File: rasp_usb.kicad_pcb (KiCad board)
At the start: 2 copper layers, 24 x 22 mm, 20 parts, among them J1 USB_B_Micro, J2 Conn_02x05_Odd_Even, U1 AMS1117-5.0, U2 FT230XQ

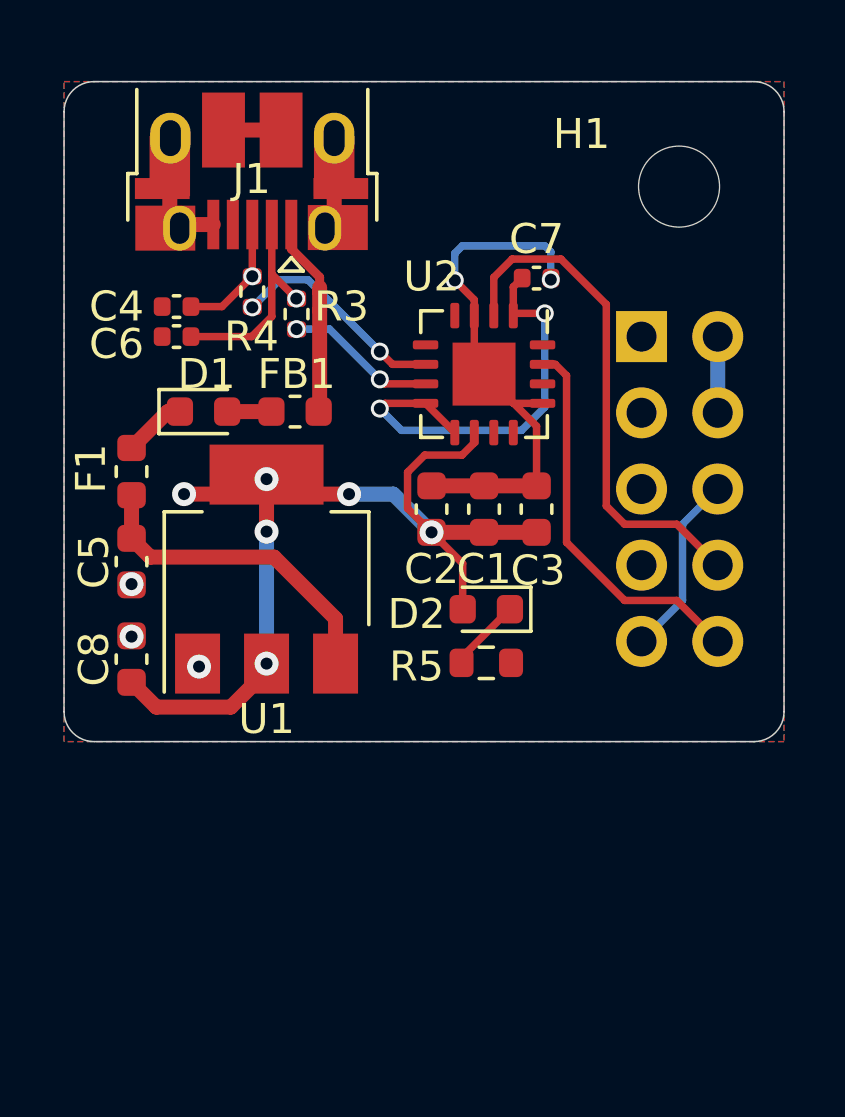
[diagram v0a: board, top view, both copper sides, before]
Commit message: ftdi ic is out of stock
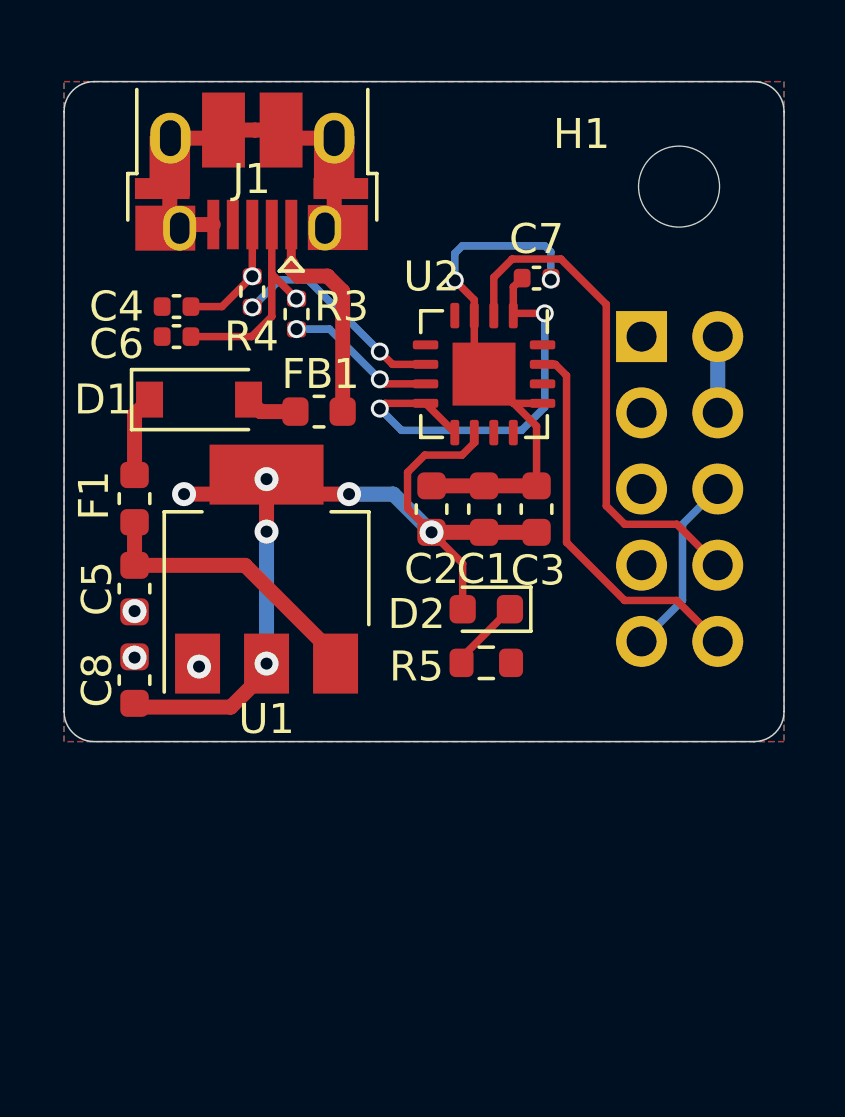
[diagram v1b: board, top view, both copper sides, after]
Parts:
- D1: footprint Diode_SMD:D_0603_1608Metric -> Diode_SMD:D_SOD-123
- moved C5 0.91 mm to (103.3, 76.9)
- moved F1 0.91 mm to (103.3, 73.9)
- moved FB1 0.80 mm to (109.5, 71.0)
- moved C8 0.71 mm to (103.3, 80.0)
- moved D1 0.43 mm to (105.5, 70.6)
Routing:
- net GND: track 33.4 -> 37.2 mm
- net Net-(C5-Pad1): track 10.9 -> 9.73 mm
- net VBUS: track 6.68 -> 7.52 mm
- net Net-(D1-Pad1): track 2.11 -> 2.72 mm

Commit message: ready to order
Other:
- board text added: "."

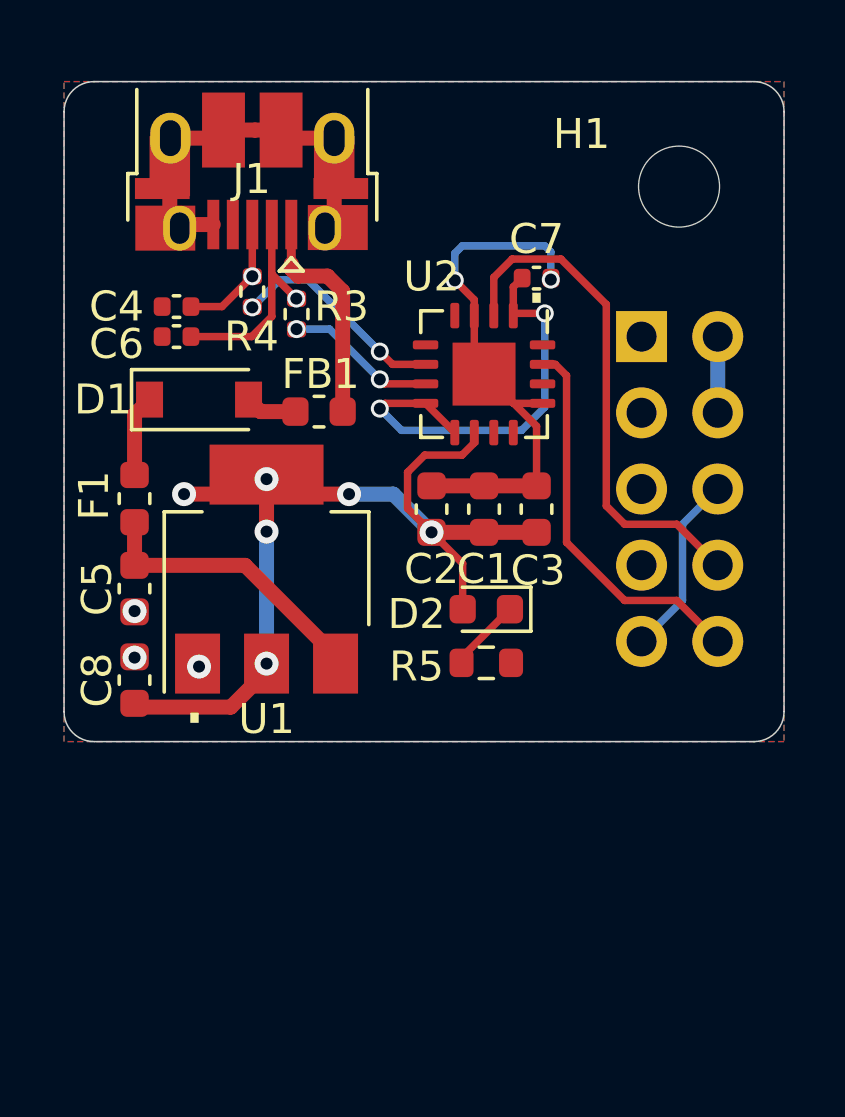
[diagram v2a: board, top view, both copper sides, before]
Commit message: Replaced usb IC with cp2104. Ready to order
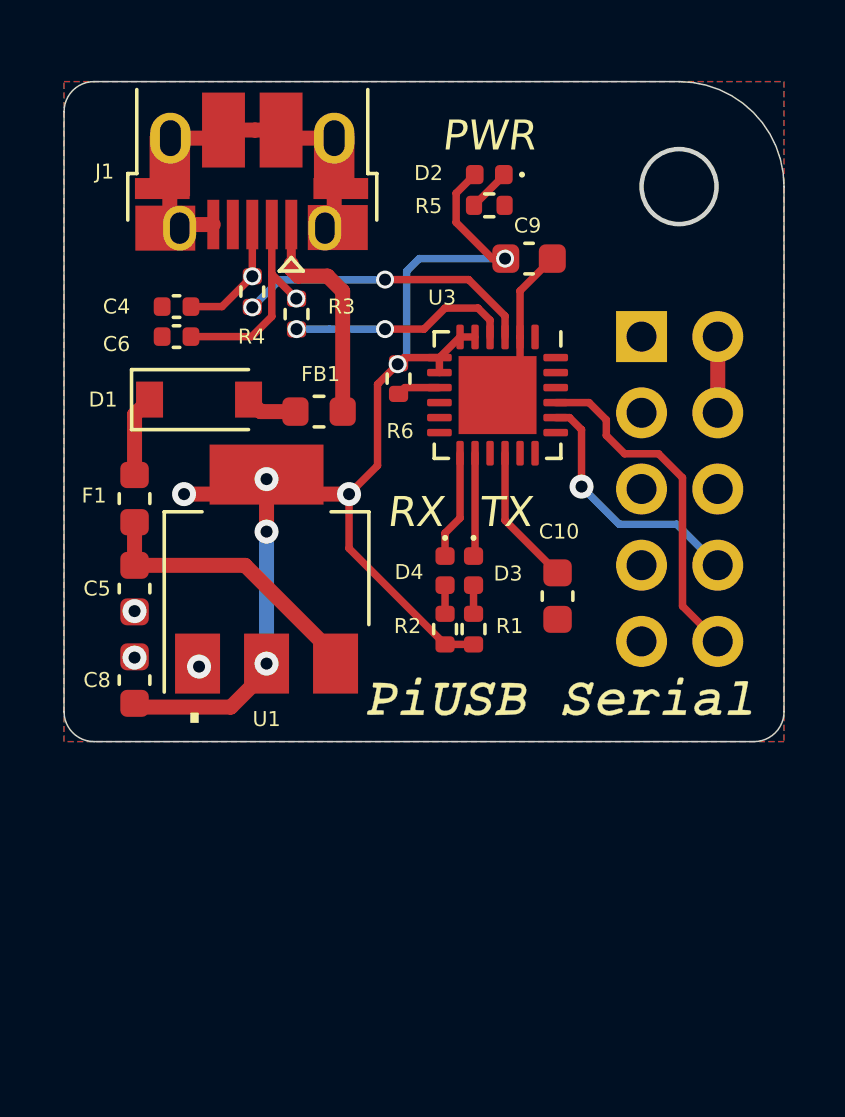
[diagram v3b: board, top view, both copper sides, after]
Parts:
- removed C1, C2: 100n, Capacitor_SMD:C_0603_1608Metric
- removed C3: 4.7u, Capacitor_SMD:C_0603_1608Metric
- removed C7: 100n, Capacitor_SMD:C_0402_1005Metric
- removed H1: MountingHole, MountingHole:MountingHole_2.7mm_M2.5
- removed U2: FT230XQ, Package_DFN_QFN:QFN-16-1EP_4x4mm_P0.65mm_EP2.1x2.1mm
- added C10: 4.7u, Capacitor_SMD:C_0603_1608Metric, F.Cu at (117.5, 77.2)
- added C9: 1u, Capacitor_SMD:C_0603_1608Metric, F.Cu at (116.5, 65.9)
- added D3: LED_TX, LED_SMD:LED_0402_1005Metric, F.Cu at (114.7, 76.3)
- added D4: LED_RX, LED_SMD:LED_0402_1005Metric, F.Cu at (113.7, 76.3)
- added G***: LOGO, logo:logo, F.Cu at (117.5, 80.5)
- added R1: 2.2k, Resistor_SMD:R_0402_1005Metric, F.Cu at (114.7, 78.2)
- added R2: 2.2k, Resistor_SMD:R_0402_1005Metric, F.Cu at (113.7, 78.2)
- added R6: 4.7k, Resistor_SMD:R_0402_1005Metric, F.Cu at (112.2, 69.9)
- added U3: CP2104, Package_DFN_QFN:QFN-24-1EP_4x4mm_P0.5mm_EP2.6x2.6mm, F.Cu at (115.5, 70.5)
- D2: value LED_Small -> LED_PWR; footprint LED_SMD:LED_0603_1608Metric -> LED_SMD:LED_0402_1005Metric
- R5: footprint Resistor_SMD:R_0603_1608Metric -> Resistor_SMD:R_0402_1005Metric
- moved R5 15.3 mm to (115.2, 64.1)
- moved D2 14.5 mm to (115.2, 63.1)
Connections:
- net +5V renamed VIO
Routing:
- net GND: track 37.2 -> 17.3 mm, vias 5 -> 3
- net Net-(C7-Pad1): track 14.7 -> 0.00 mm, vias 2 -> 0
- net VIO: track 32.6 -> 44.2 mm, vias 6 -> 7
- net UART_TXD: track 17.2 -> 8.55 mm, vias 0 -> 1
- net Net-(C10-Pad1): track 0.00 -> 4.71 mm
- net Net-(D4-Pad1): track 0.00 -> 3.63 mm
- net Net-(D3-Pad1): track 0.00 -> 3.45 mm
- net Net-(R4-Pad2): track 7.32 -> 10.0 mm
- net Net-(R3-Pad2): track 5.06 -> 7.47 mm
- net Net-(R6-Pad2): track 0.00 -> 1.45 mm
- net UART_RXD: track 12.9 -> 11.5 mm
- net Net-(D2-Pad1): track 2.46 -> 1.44 mm
- net Net-(D4-Pad2): track 0.00 -> 0.95 mm
- net Net-(D3-Pad2): track 0.00 -> 0.95 mm
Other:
- outline, holes or cut-outs redrawn
- board text added: "PWR"
- board text added: "RX"
- board text added: "TX"

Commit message: ready to order
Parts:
- J1: footprint Connector_USB:USB_Micro-B_Amphenol_10103594-0001LF_Horizontal -> Connector_USB:USB_Micro-B_Amphenol_10104110_Horizontal
- moved J1 1.35 mm to (107.8, 64.2)
- moved R4 1.25 mm to (107.2, 68.2)
- moved R3 1.00 mm to (108.8, 68.8)
- moved C4 0.25 mm to (104.8, 67.8)
- moved C6 0.25 mm to (104.8, 68.8)
- moved G*** 0.25 mm to (117.2, 80.5)
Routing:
- net VBUS: track 7.52 -> 5.70 mm, vias 0 -> 2
- net GND: track 17.3 -> 15.7 mm
- net Net-(R4-Pad2): track 10.0 -> 10.8 mm
- net USB_DM: track 7.20 -> 6.84 mm, vias 1 -> 0
- net USB_DP: track 4.19 -> 4.17 mm, vias 1 -> 0

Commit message: thin board
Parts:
- moved D2 23.7 mm to (108.6, 85.8), turned to 270 degrees
- moved R5 22.4 mm to (109.6, 85.8), turned to 90 degrees
- moved C9 19.3 mm to (111.4, 84.5), turned to 90 degrees
- moved R6 18.2 mm to (115.5, 87.8), turned to 0 degrees
- moved U3 13.9 mm to (116.0, 84.3), turned to 0 degrees
- moved D3 13.4 mm to (122.1, 87.5), turned to 90 degrees
- moved D4 13.1 mm to (120.5, 87.5), turned to 90 degrees
- moved R1 10.4 mm to (122.1, 85.5), turned to 270 degrees
- moved G*** 10.0 mm to (116.2, 90.5)
- moved R2 9.97 mm to (120.5, 85.5), turned to 90 degrees
- moved C10 7.67 mm to (121.8, 83.5), turned to 0 degrees
- moved J1 6.29 mm to (114.0, 63.5)
- moved C4 6.27 mm to (111.0, 67.2)
- moved C5 6.27 mm to (109.6, 76.4)
- moved C6 6.27 mm to (111.0, 68.2)
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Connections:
- C8 pad 1: VIO -> 5V
- C9 pad 1: VIO -> 5V
- D2 pad 2: VIO -> 5V
- R1 pad 1: VIO -> 5V
- R2 pad 2: VIO -> 5V
- R6 pad 1: VIO -> 5V
- U1 pad 2: VIO -> 5V
- U3 pad 5: VIO -> 5V
- U3 pad 6: VIO -> 5V
- U3 pad 7: VIO -> 5V
- U3 pad 8: VIO -> 5V
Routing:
- net 5V: track 2.54 -> 68.4 mm, vias 0 -> 9
- net VIO: track 44.2 -> 0.00 mm, vias 7 -> 0
- net Net-(R3-Pad2): track 7.89 -> 20.0 mm
- net Net-(R4-Pad2): track 10.8 -> 17.2 mm
- net GND: track 15.7 -> 18.7 mm, vias 3 -> 5
- net Net-(D3-Pad1): track 3.45 -> 6.11 mm, vias 0 -> 2
- net UART_RXD: track 11.5 -> 8.89 mm, vias 0 -> 1
- net UART_TXD: track 8.55 -> 10.5 mm, vias 1 -> 0
- net Net-(C10-Pad1): track 4.71 -> 3.32 mm
- net Net-(D4-Pad1): track 3.63 -> 4.29 mm
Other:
- board size 24 x 22 mm -> 17.5 x 32.5 mm

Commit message: annotation number
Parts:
- moved D4 0.40 mm to (121.0, 87.5)
- moved R2 0.40 mm to (121.0, 85.5)
- moved G*** 0.08 mm to (116.3, 90.5)
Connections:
- net 3V3 renamed +3V3
- net 5V renamed +5V
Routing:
- net +5V: track 68.4 -> 67.9 mm

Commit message: Ready to order
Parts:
- moved G*** 1.33 mm to (115.0, 90.5)
- moved C10 1.00 mm to (120.8, 83.5)
- moved C4 1.00 mm to (110.0, 67.2)
- moved C5 1.00 mm to (108.6, 76.4)
- moved C6 1.00 mm to (110.0, 68.2)
- moved C8 1.00 mm to (108.6, 79.5)
- moved C9 1.00 mm to (110.4, 84.5)
- moved D1 1.00 mm to (110.8, 70.1)
- moved D2 1.00 mm to (107.6, 85.8)
- moved D3 1.00 mm to (121.1, 87.5)
- moved D4 1.00 mm to (120.0, 87.5)
- moved F1 1.00 mm to (108.6, 73.4)
- moved FB1 1.00 mm to (114.8, 70.5)
- moved J1 1.00 mm to (113.0, 63.5)
- moved R1 1.00 mm to (121.1, 85.5)
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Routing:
- net UART_RXD: track 8.89 -> 9.89 mm
- net UART_TXD: track 10.5 -> 11.2 mm
- net +5V: track 67.9 -> 67.3 mm
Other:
- board size 17.5 x 32.5 mm -> 20 x 32.5 mm
